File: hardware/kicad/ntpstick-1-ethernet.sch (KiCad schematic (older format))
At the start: 38 parts, among them IC1 W5500, P1 EIA 568B, U1 TG110-E*N5_N5, X1 25MHz

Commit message: Version 1.2 HW design
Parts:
- C11, C5: footprint Capacitors_Tantalum_SMD:TantalC_SizeA_EIA-3216_Reflow -> Water SMD Cap:c_tant_A
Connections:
- net labels added: RX1_N, RX1_P, RX_N, RX_P, TX_N, TX_P
- net labels removed: RXN, RXP, TXN, TXP
- wire segments 134 -> 171
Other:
- moved on the sheet: D1, R4

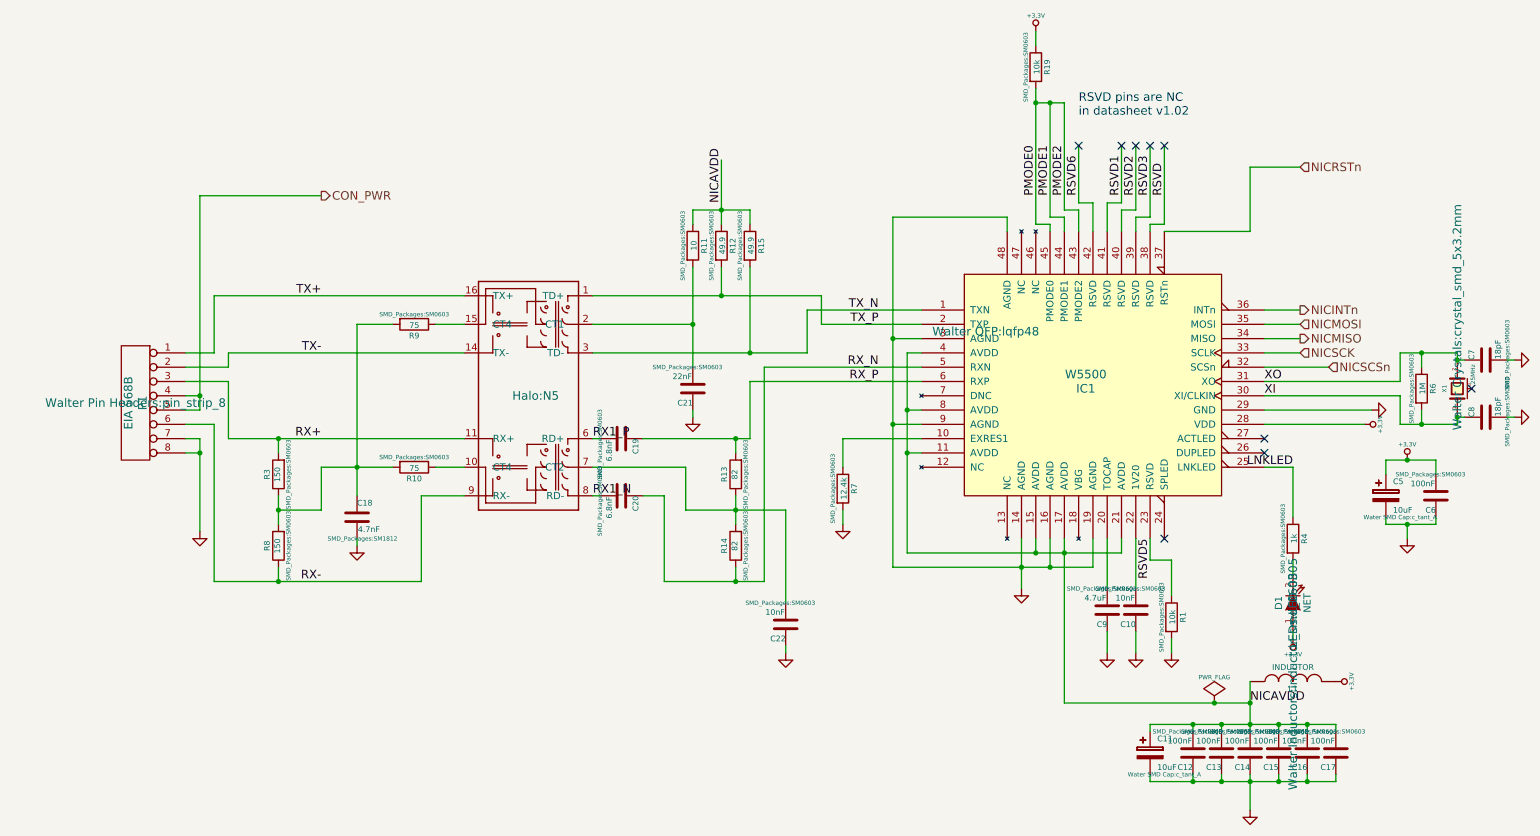
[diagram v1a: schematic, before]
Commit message: Final manufactured version of 1.2 HW
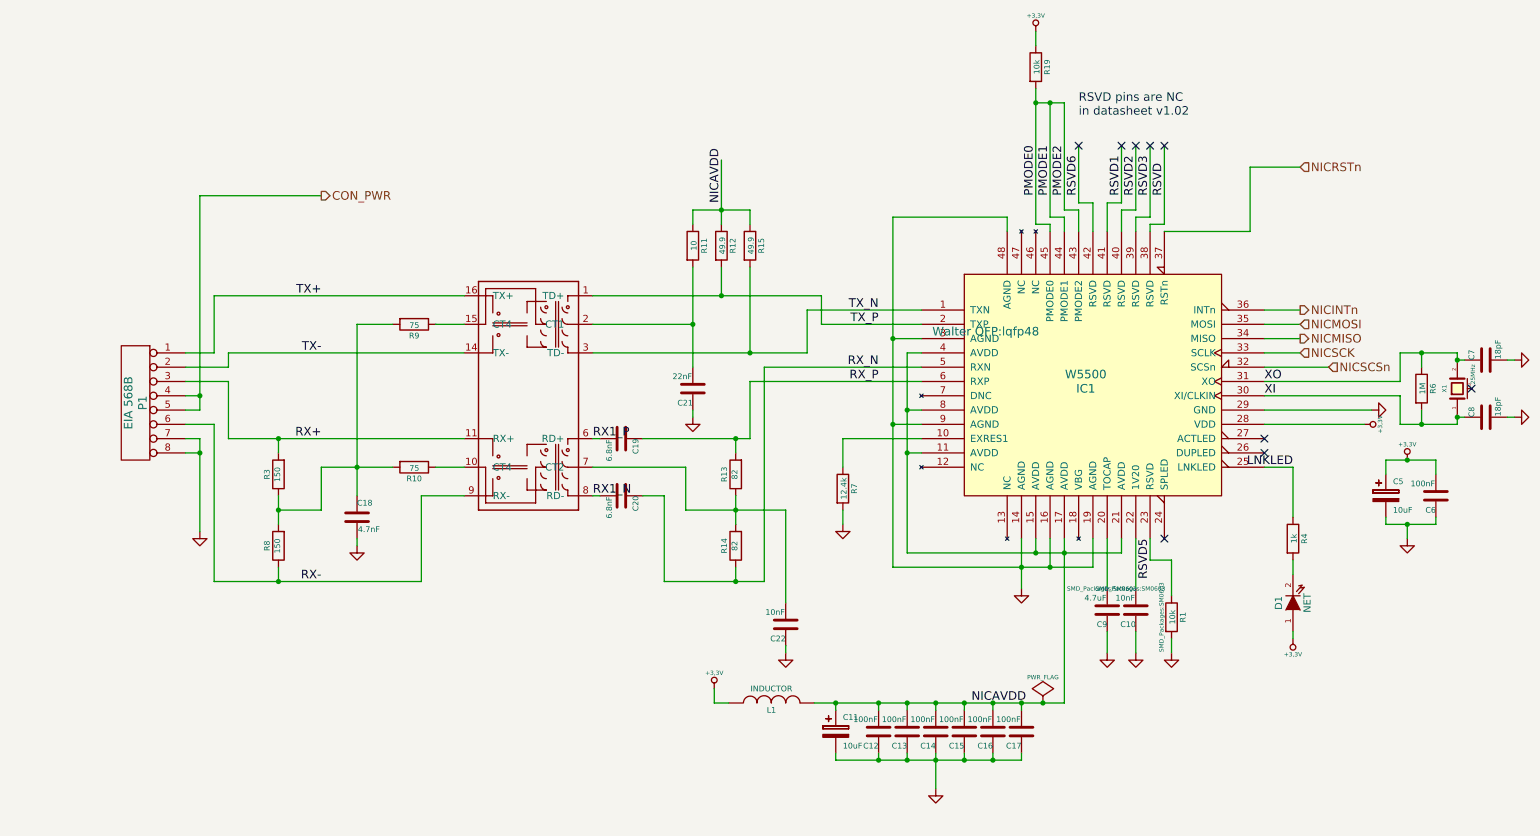
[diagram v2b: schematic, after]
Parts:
- L1: footprint Walter Inductors:inductor_smd_0603 -> SMD_Packages:SM0603
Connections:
- net +3.3V: now also L1.1; no longer L1.2
- net NICAVDD: now also L1.2; no longer L1.1
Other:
- moved on the sheet: C11, C12, C13, C14, C15, C16, C17, L1
